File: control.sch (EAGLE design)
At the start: 4 parts, among them J1 1-2328702-0, U2 ESP32-DEVKITC-32D

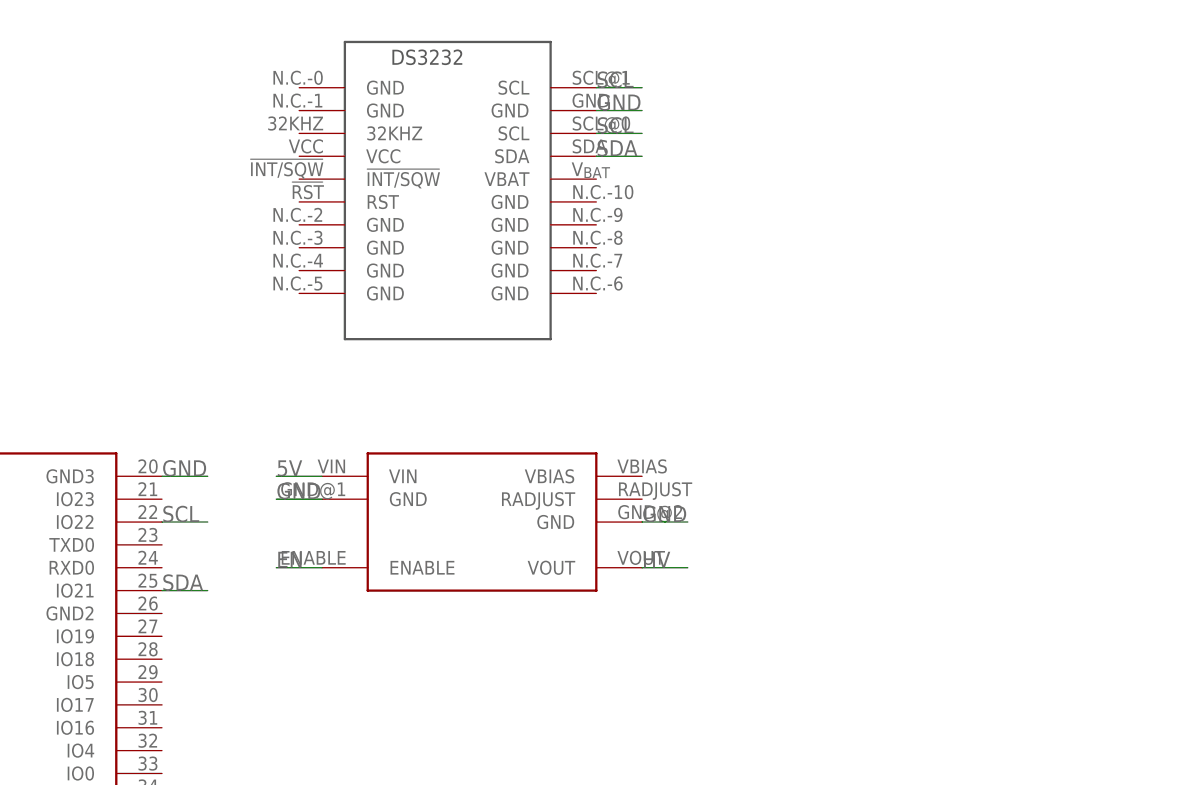
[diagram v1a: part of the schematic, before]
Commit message: add readme, brushup board
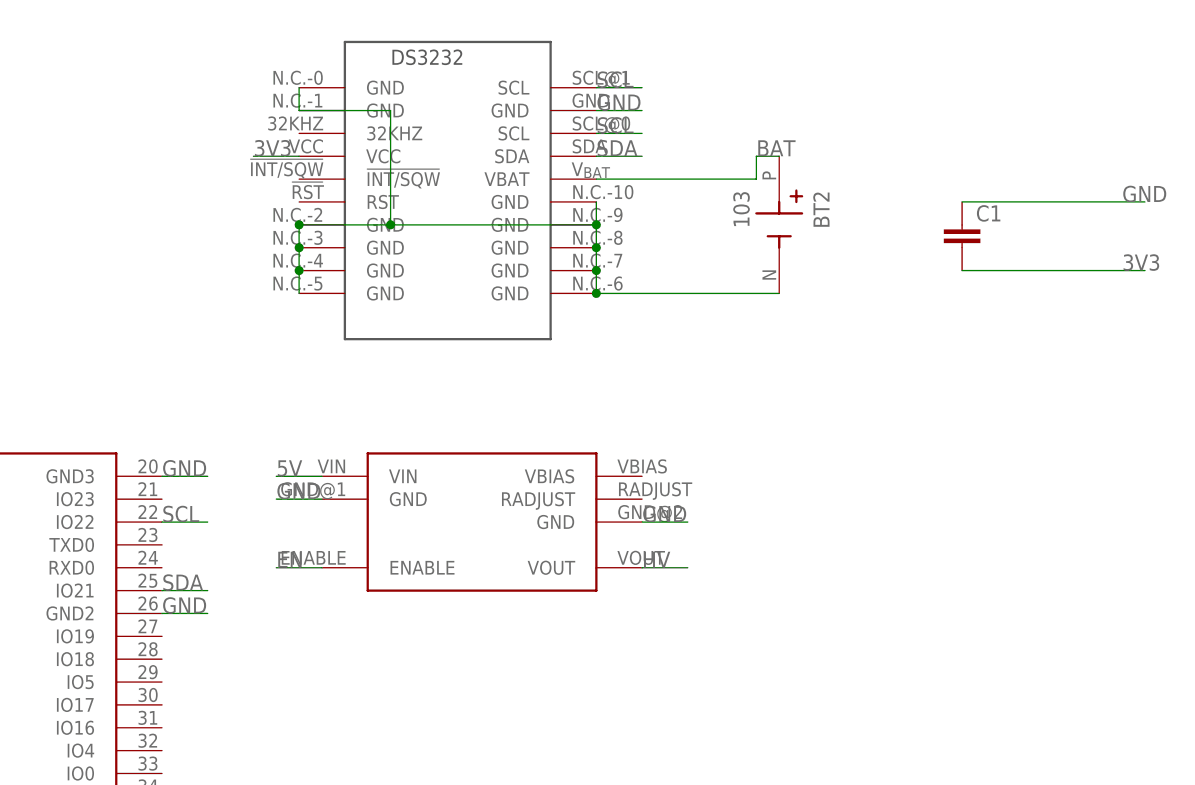
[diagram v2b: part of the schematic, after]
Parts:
- added BT2: 103, 103:103
- added C1: (no value), rcl:C-EUC0805
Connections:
- new net BAT: BT2.POS, U$1.VBAT
- net 3V3: now also C1.2, U$1.VCC
- net GND: now also BT2.NEG, C1.1, U$1.GND@0, U$1.GND@1, U$1.GND@10, U$1.GND@2, U$1.GND@3, U$1.GND@4, U$1.GND@5, U$1.GND@6, U$1.GND@7, U$1.GND@8, U$1.GND@9, U2.GND2
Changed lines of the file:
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@@
 <part name="U2" library="SamacSys_Parts" deviceset="ESP32-DEVKITC-32D" device="" package3d_urn="urn:adsk.eagle:package:22471105/5"/>
 <part name="J1" library="1-2328702-0" deviceset="1-2328702-0" device=""/>
+<part name="BT2" library="103" deviceset="103" device=""/>
+<part name="C1" library="rcl" library_urn="urn:adsk.eagle:library:334" deviceset="C-EU" device="C0805" package3d_urn="urn:adsk.eagle:package:23617/2"/>
 </parts>
 <sheets>
@@
 <attribute name="VALUE" x="177.8" y="104.14" size="1.778" layer="96"/>
 </instance>
+<instance part="BT2" gate="G$1" x="281.94" y="116.84" smashed="yes" rot="R270">
+<attribute name="NAME" x="285.75" y="120.65" size="1.778" layer="95" rot="R270"/>
+<attribute name="VALUE" x="276.86" y="120.65" size="1.778" layer="96" rot="R270"/>
+</instance>
+<instance part="C1" gate="G$1" x="302.26" y="116.84" smashed="yes">
+<attribute name="NAME" x="303.784" y="117.221" size="1.778" layer="95"/>
+<attribute name="VALUE" x="303.784" y="112.141" size="1.778" layer="96"/>
+</instance>
 </instances>
 <busses>
@@
 <pinref part="U2" gate="G$1" pin="IO32"/>
 </segment>
+<segment>
+<pinref part="C1" gate="G$1" pin="1"/>
+<wire x1="322.58" y1="119.38" x2="302.26" y2="119.38" width="0.1524" layer="91"/>
+<label x="320.04" y="119.38" size="1.778" layer="95"/>
+</segment>
+<segment>
+<pinref part="U$1" gate="G$1" pin="GND@0"/>
+<pinref part="U$1" gate="G$1" pin="GND@1"/>
+<wire x1="228.6" y1="132.08" x2="228.6" y2="129.54" width="0.1524" layer="91"/>
+<wire x1="228.6" y1="129.54" x2="238.76" y2="129.54" width="0.1524" layer="91"/>
+<pinref part="U$1" gate="G$1" pin="GND@2"/>
+<pinref part="U$1" gate="G$1" pin="GND@3"/>
+<wire x1="228.6" y1="116.84" x2="228.6" y2="114.3" width="0.1524" layer="91"/>
+<pinref part="U$1" gate="G$1" pin="GND@4"/>
+<wire x1="228.6" y1="114.3" x2="228.6" y2="111.76" width="0.1524" layer="91"/>
+<junction x="228.6" y="114.3"/>
+<pinref part="U$1" gate="G$1" pin="GND@5"/>
+<wire x1="228.6" y1="111.76" x2="228.6" y2="109.22" width="0.1524" layer="91"/>
+<junction x="228.6" y="111.76"/>
+<wire x1="238.76" y1="129.54" x2="238.76" y2="116.84" width="0.1524" layer="91"/>
+<wire x1="238.76" y1="116.84" x2="228.6" y2="116.84" width="0.1524" layer="91"/>
+<junction x="228.6" y="116.84"/>
+<pinref part="U$1" gate="G$1" pin="GND@10"/>
+<pinref part="U$1" gate="G$1" pin="GND@6"/>
+<wire x1="261.62" y1="119.38" x2="261.62" y2="116.84" width="0.1524" layer="91"/>
+<pinref part="U$1" gate="G$1" pin="GND@7"/>
+<wire x1="261.62" y1="116.84" x2="261.62" y2="114.3" width="0.1524" layer="91"/>
+<wire x1="261.62" y1="114.3" x2="261.62" y2="111.76" width="0.1524" layer="91"/>
+<wire x1="261.62" y1="111.76" x2="261.62" y2="109.22" width="0.1524" layer="91"/>
+<junction x="261.62" y="111.76"/>
+<pinref part="U$1" gate="G$1" pin="GND@8"/>
+<junction x="261.62" y="114.3"/>
+<pinref part="U$1" gate="G$1" pin="GND@9"/>
+<junction x="261.62" y="116.84"/>
+<pinref part="BT2" gate="G$1" pin="NEG"/>
+<wire x1="261.62" y1="109.22" x2="281.94" y2="109.22" width="0.1524" layer="91"/>
+<junction x="261.62" y="109.22"/>
+<wire x1="238.76" y1="116.84" x2="261.62" y2="116.84" width="0.1524" layer="91"/>
+<junction x="238.76" y="116.84"/>
+</segment>
+<segment>
+<wire x1="213.36" y1="73.66" x2="218.44" y2="73.66" width="0.1524" layer="91"/>
+<label x="213.36" y="73.66" size="1.778" layer="95"/>
+<pinref part="U2" gate="G$1" pin="GND2"/>
+</segment>
 </net>
 <net name="3V3" class="0">
@@
 <pinref part="U2" gate="G$1" pin="IO33"/>
 </segment>
+<segment>
+<pinref part="C1" gate="G$1" pin="2"/>
+<wire x1="302.26" y1="111.76" x2="322.58" y2="111.76" width="0.1524" layer="91"/>
+<label x="320.04" y="111.76" size="1.778" layer="95"/>
+</segment>
+<segment>
+<wire x1="223.52" y1="124.46" x2="228.6" y2="124.46" width="0.1524" layer="91"/>
+<label x="223.52" y="124.46" size="1.778" layer="95"/>
+<pinref part="U$1" gate="G$1" pin="VCC"/>
+</segment>
 </net>
 <net name="HV" class="0">
@@
 <label x="213.36" y="76.2" size="1.778" layer="95"/>
 <pinref part="U2" gate="G$1" pin="IO21"/>
+</segment>
+</net>
+<net name="BAT" class="0">
+<segment>
+<pinref part="U$1" gate="G$1" pin="VBAT"/>
+<wire x1="261.62" y1="121.92" x2="279.4" y2="121.92" width="0.1524" layer="91"/>
+<wire x1="279.4" y1="121.92" x2="279.4" y2="124.46" width="0.1524" layer="91"/>
+<pinref part="BT2" gate="G$1" pin="POS"/>
+<wire x1="279.4" y1="124.46" x2="281.94" y2="124.46" width="0.1524" layer="91"/>
+<label x="279.4" y="124.46" size="1.778" layer="95"/>
 </segment>
 </net>
@@
 </drawing>
 <compatibility>
+<note version="8.2" severity="warning">
+Since Version 8.2, EAGLE supports online libraries. The ids
+of those online libraries will not be understood (or retained)
+with this version.
+</note>
 <note version="8.3" severity="warning">
 Since Version 8.3, EAGLE supports URNs for individual library

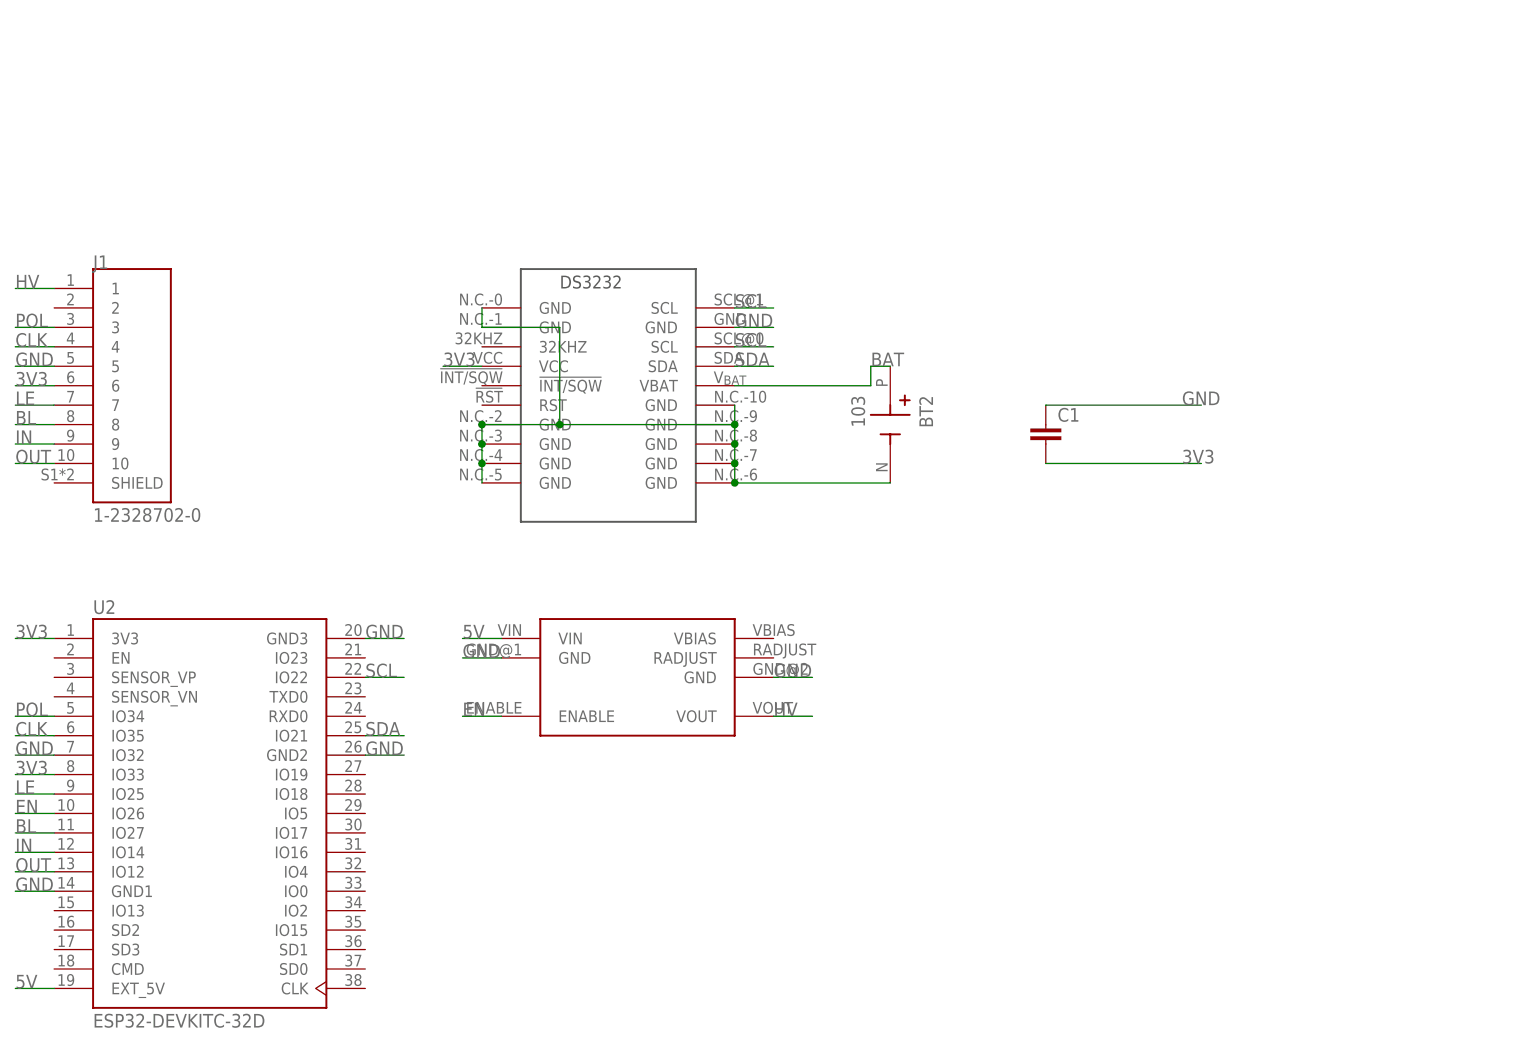
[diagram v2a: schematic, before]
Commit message: added potentio, readme update
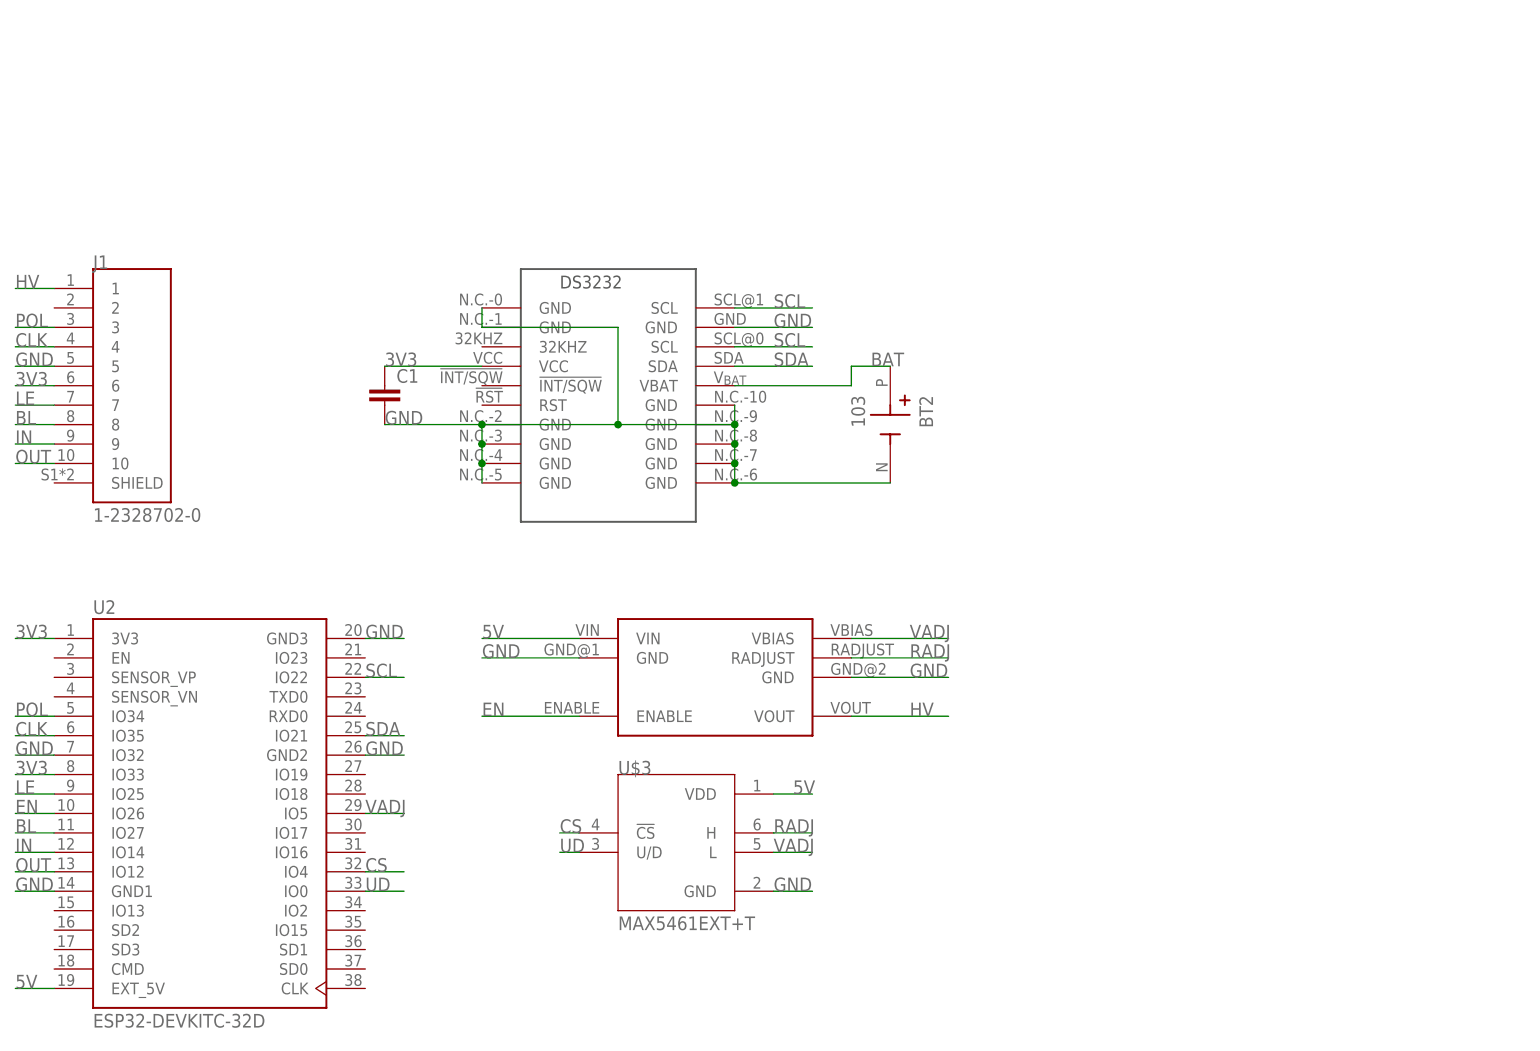
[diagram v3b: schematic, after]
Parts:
- added U$3: MAX5461EXT+T, MAX5461EXT_T:MAX5461EXT+T
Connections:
- new net CS: U$3.!CS, U2.IO4
- new net RADJ: U$2.RADJUST, U$3.H
- new net UD: U$3.U/D, U2.IO0
- new net VADJ: U$2.VBIAS, U$3.L, U2.IO5
- net 3V3: now also C1.1; no longer C1.2
- net 5V: now also U$3.VDD
- net GND: now also C1.2, U$3.GND; no longer C1.1
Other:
- moved on the sheet: C1

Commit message: reg update
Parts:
- added C2: 0.1u, rcl:C-EUC0805
- added C3, C4, C5: 100u, rcl:C-EUC1210
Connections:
- net 5V: now also C2.1, C3.2, C4.2, C5.2
- net GND: now also C2.2, C3.1, C4.1, C5.1
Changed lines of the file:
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@@
 <part name="C1" library="rcl" library_urn="urn:adsk.eagle:library:334" deviceset="C-EU" device="C0805" package3d_urn="urn:adsk.eagle:package:23617/2"/>
 <part name="U$3" library="MAX5461EXT_T" deviceset="MAX5461EXT+T" device=""/>
+<part name="C2" library="rcl" library_urn="urn:adsk.eagle:library:334" deviceset="C-EU" device="C0805" package3d_urn="urn:adsk.eagle:package:23617/2" value="0.1u"/>
+<part name="C3" library="rcl" library_urn="urn:adsk.eagle:library:334" deviceset="C-EU" device="C1210" package3d_urn="urn:adsk.eagle:package:23619/2" value="100u"/>
+<part name="C4" library="rcl" library_urn="urn:adsk.eagle:library:334" deviceset="C-EU" device="C1210" package3d_urn="urn:adsk.eagle:package:23619/2" value="100u"/>
+<part name="C5" library="rcl" library_urn="urn:adsk.eagle:library:334" deviceset="C-EU" device="C1210" package3d_urn="urn:adsk.eagle:package:23619/2" value="100u"/>
 </parts>
 <sheets>
@@
 <attribute name="VALUE" x="246.38" y="50.8" size="1.778" layer="96"/>
 </instance>
+<instance part="C2" gate="G$1" x="279.4" y="60.96" smashed="yes">
+<attribute name="NAME" x="280.924" y="61.341" size="1.778" layer="95"/>
+<attribute name="VALUE" x="280.924" y="56.261" size="1.778" layer="96"/>
+</instance>
+<instance part="C3" gate="G$1" x="228.6" y="99.06" smashed="yes">
+<attribute name="NAME" x="230.124" y="99.441" size="1.778" layer="95"/>
+<attribute name="VALUE" x="230.124" y="94.361" size="1.778" layer="96"/>
+</instance>
+<instance part="C4" gate="G$1" x="236.22" y="99.06" smashed="yes">
+<attribute name="NAME" x="237.744" y="99.441" size="1.778" layer="95"/>
+<attribute name="VALUE" x="237.744" y="94.361" size="1.778" layer="96"/>
+</instance>
+<instance part="C5" gate="G$1" x="243.84" y="99.06" smashed="yes">
+<attribute name="NAME" x="245.364" y="99.441" size="1.778" layer="95"/>
+<attribute name="VALUE" x="245.364" y="94.361" size="1.778" layer="96"/>
+</instance>
 </instances>
 <busses>
@@
 <label x="228.6" y="88.9" size="1.778" layer="95"/>
 <pinref part="U$2" gate="G$1" pin="VIN"/>
+<pinref part="C3" gate="G$1" pin="2"/>
+<pinref part="C4" gate="G$1" pin="2"/>
+<wire x1="228.6" y1="93.98" x2="236.22" y2="93.98" width="0.1524" layer="91"/>
+<pinref part="C5" gate="G$1" pin="2"/>
+<wire x1="236.22" y1="93.98" x2="243.84" y2="93.98" width="0.1524" layer="91"/>
+<junction x="236.22" y="93.98"/>
+<wire x1="228.6" y1="93.98" x2="228.6" y2="88.9" width="0.1524" layer="91"/>
+<junction x="228.6" y="93.98"/>
 </segment>
 <segment>
-<wire x1="271.78" y1="68.58" x2="266.7" y2="68.58" width="0.1524" layer="91"/>
 <label x="269.24" y="68.58" size="1.778" layer="95"/>
 <pinref part="U$3" gate="G$1" pin="VDD"/>
+<wire x1="266.7" y1="68.58" x2="279.4" y2="68.58" width="0.1524" layer="91"/>
+<pinref part="C2" gate="G$1" pin="1"/>
+<wire x1="279.4" y1="68.58" x2="279.4" y2="63.5" width="0.1524" layer="91"/>
 </segment>
 </net>
@@
 </segment>
 <segment>
-<wire x1="228.6" y1="86.36" x2="241.3" y2="86.36" width="0.1524" layer="91"/>
+<wire x1="223.52" y1="86.36" x2="241.3" y2="86.36" width="0.1524" layer="91"/>
 <label x="228.6" y="86.36" size="1.778" layer="95"/>
 <pinref part="U$2" gate="G$1" pin="GND@1"/>
+<pinref part="C3" gate="G$1" pin="1"/>
+<pinref part="C4" gate="G$1" pin="1"/>
+<wire x1="228.6" y1="101.6" x2="236.22" y2="101.6" width="0.1524" layer="91"/>
+<pinref part="C5" gate="G$1" pin="1"/>
+<wire x1="236.22" y1="101.6" x2="243.84" y2="101.6" width="0.1524" layer="91"/>
+<junction x="236.22" y="101.6"/>
+<wire x1="228.6" y1="101.6" x2="223.52" y2="101.6" width="0.1524" layer="91"/>
+<junction x="228.6" y="101.6"/>
+<wire x1="223.52" y1="101.6" x2="223.52" y2="86.36" width="0.1524" layer="91"/>
 </segment>
 <segment>
@@
 </segment>
 <segment>
-<wire x1="266.7" y1="55.88" x2="271.78" y2="55.88" width="0.1524" layer="91"/>
 <label x="266.7" y="55.88" size="1.778" layer="95"/>
 <pinref part="U$3" gate="G$1" pin="GND"/>
+<pinref part="C2" gate="G$1" pin="2"/>
+<wire x1="266.7" y1="55.88" x2="279.4" y2="55.88" width="0.1524" layer="91"/>
 </segment>
 </net>
